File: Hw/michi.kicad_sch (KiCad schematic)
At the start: 52 parts, among them J1 Conn_01x02, J2 Conn_Right, P1 USB_C_Plug_USB2.0, SW1 SW_Push, U1 RP2040, U2 NCP1117ST33T3G, U3 W25Q128JVS, Y1 Crystal

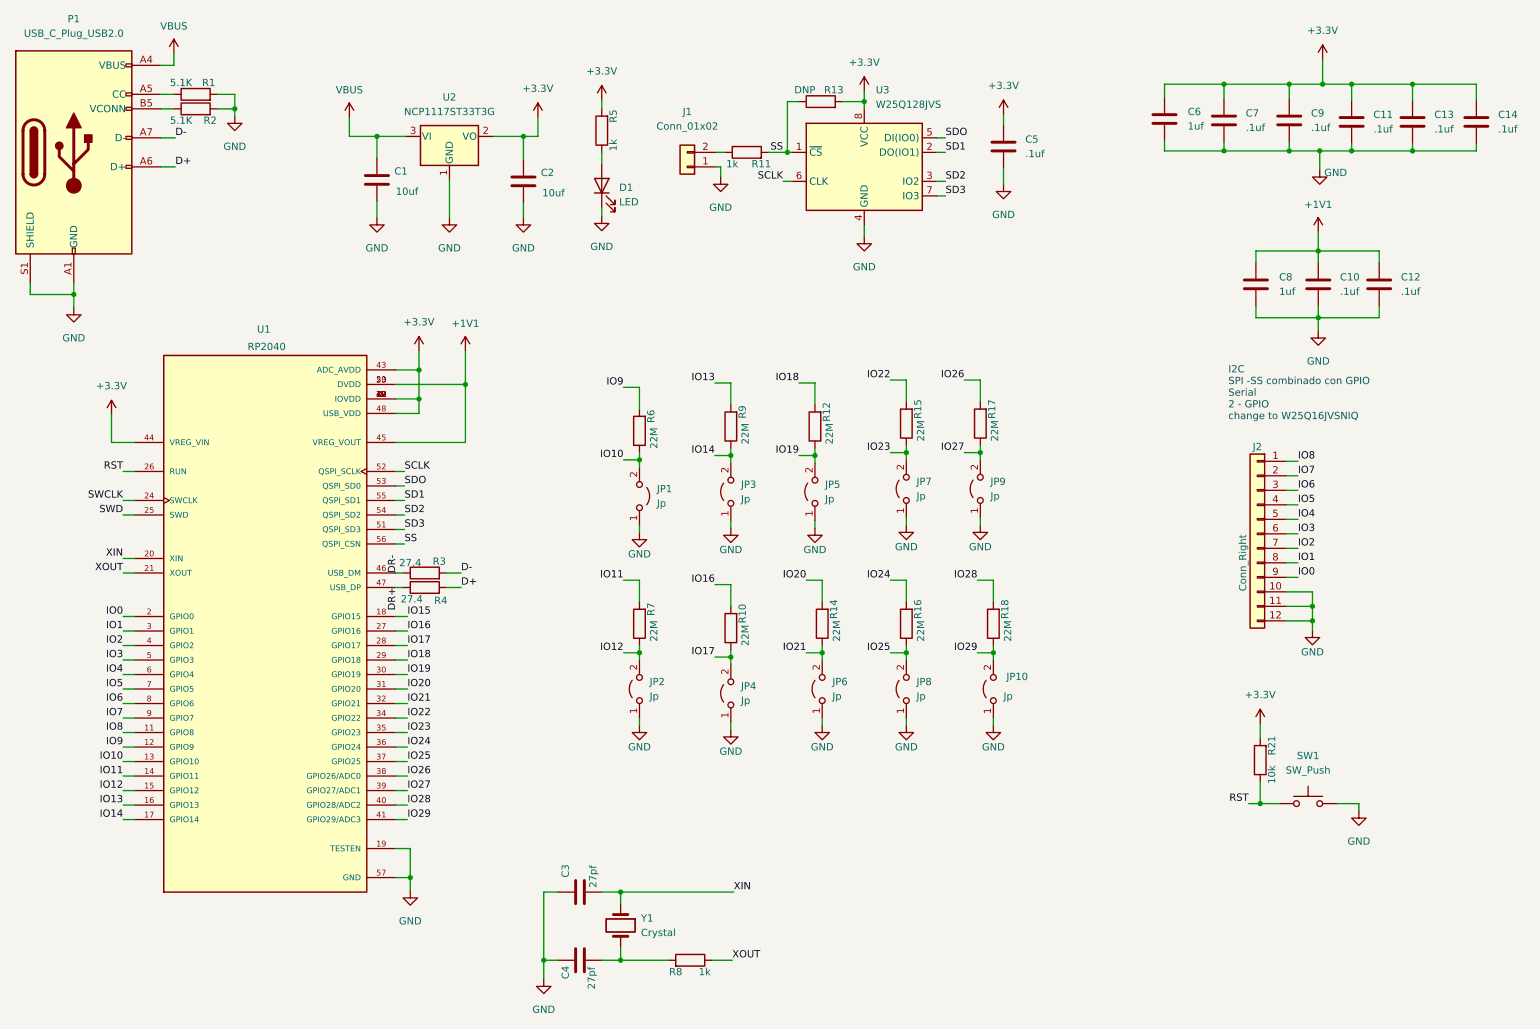
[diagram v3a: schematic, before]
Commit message: fix footprints
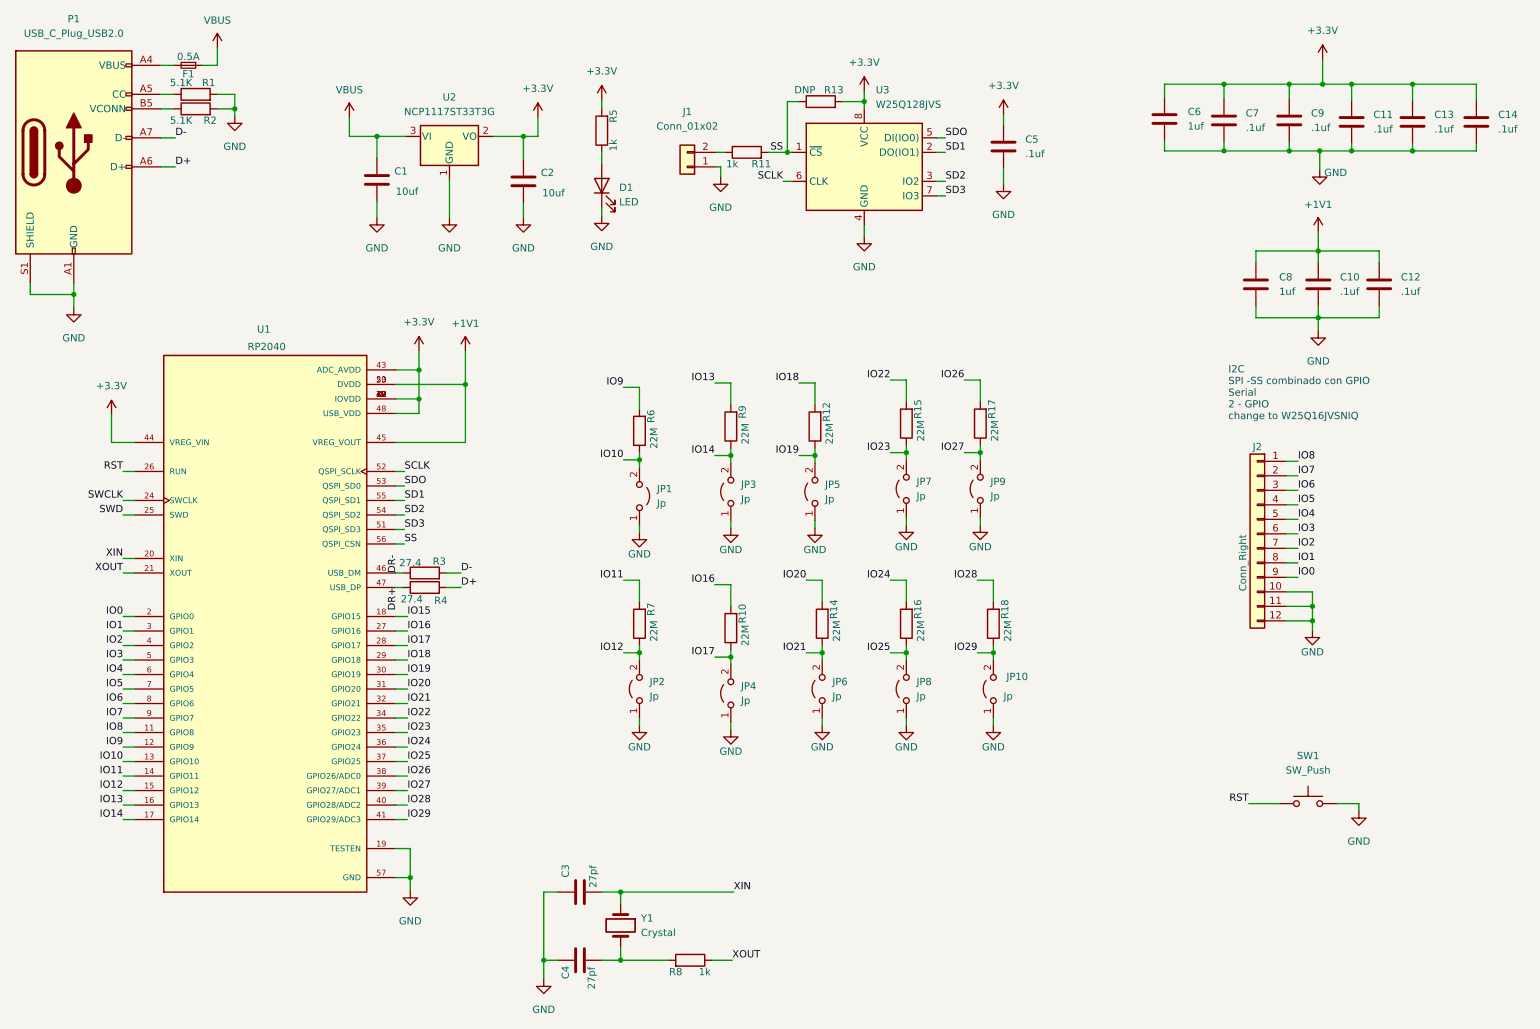
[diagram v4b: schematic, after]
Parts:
- removed R21: 10k, Resistor_SMD:R_0603_1608Metric, symbol Device:R
- added F1: 0.5A, Fuse:Fuse_1812_4532Metric_Pad1.30x3.40mm_HandSolder, symbol Device:Fuse_Small
- U3: footprint Package_SO:SOIC-8_5.23x5.23mm_P1.27mm -> Library:W25Q16JVUUIQ; Manuf W25Q128JVSIM TR -> W25Q16JVUUIQ
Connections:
- net VBUS: now also F1.1; no longer P1.A4 (VBUS), P1.A9 (VBUS), P1.B4 (VBUS), P1.B9 (VBUS)
- new net: F1.2, P1.A4 (VBUS), P1.A9 (VBUS), P1.B4 (VBUS), P1.B9 (VBUS)
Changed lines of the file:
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@@
   (junction (at 245.618 118.364) (diameter 0) (color 0 0 0 0)
   )
-  (junction (at 236.474 152.908) (diameter 0) (color 0 0 0 0)
-  )
   (junction (at 245.618 120.904) (diameter 0) (color 0 0 0 0)
   )
@@
     (stroke (width 0) (type default) (color 0 0 0 0))
   )
+  (wire (pts (xy 53.848 20.574) (xy 53.848 23.622))
+    (stroke (width 0) (type default) (color 0 0 0 0))
+  )
   (wire (pts (xy 241.046 95.504) (xy 243.078 95.504))
     (stroke (width 0) (type default) (color 0 0 0 0))
@@
     (stroke (width 0) (type default) (color 0 0 0 0))
   )
-  (wire (pts (xy 236.474 149.098) (xy 236.474 152.908))
-    (stroke (width 0) (type default) (color 0 0 0 0))
-  )
   (wire (pts (xy 191.516 32.258) (xy 191.516 34.036))
     (stroke (width 0) (type default) (color 0 0 0 0))
@@
     (stroke (width 0) (type default) (color 0 0 0 0))
   )
-  (wire (pts (xy 46.228 23.622) (xy 46.228 21.59))
-    (stroke (width 0) (type default) (color 0 0 0 0))
-  )
   (wire (pts (xy 171.704 78.74) (xy 174.498 78.74))
     (stroke (width 0) (type default) (color 0 0 0 0))
@@
     (stroke (width 0) (type default) (color 0 0 0 0))
   )
+  (wire (pts (xy 53.848 23.622) (xy 51.308 23.622))
+    (stroke (width 0) (type default) (color 0 0 0 0))
+  )
   (wire (pts (xy 127.762 126.492) (xy 127.762 127.762))
     (stroke (width 0) (type default) (color 0 0 0 0))
@@
     (stroke (width 0) (type default) (color 0 0 0 0))
   )
-  (wire (pts (xy 234.442 152.908) (xy 236.474 152.908))
+  (wire (pts (xy 234.442 152.908) (xy 239.776 152.908))
     (stroke (width 0) (type default) (color 0 0 0 0))
   )
@@
     (stroke (width 0) (type default) (color 0 0 0 0))
   )
-  (wire (pts (xy 236.474 152.908) (xy 239.776 152.908))
-    (stroke (width 0) (type default) (color 0 0 0 0))
-  )
   (wire (pts (xy 37.338 132.842) (xy 39.37 132.842))
     (stroke (width 0) (type default) (color 0 0 0 0))
@@
     (stroke (width 0) (type default) (color 0 0 0 0))
   )
-  (wire (pts (xy 236.474 138.938) (xy 236.474 141.478))
-    (stroke (width 0) (type default) (color 0 0 0 0))
-  )
   (wire (pts (xy 85.09 94.742) (xy 86.614 94.742))
     (stroke (width 0) (type default) (color 0 0 0 0))
@@
     (pin "1")
   )
+  (symbol (lib_id "Device:Fuse_Small") (at 48.768 23.622 0) (mirror y) (unit 1)
+    (in_bom yes) (on_board yes)
+    (property "Reference" "F1" (id 0) (at 48.768 25.146 0))
+    (property "Value" "0.5A" (id 1) (at 48.768 22.098 0))
+    (property "Footprint" "Fuse:Fuse_1812_4532Metric_Pad1.30x3.40mm_HandSolder" (id 2) (at 48.768 23.622 0)
+      (effects (font (size 1.27 1.27)) hide)
+    )
+    (property "Datasheet" "" (id 3) (at 48.768 23.622 0))
+    (property "Part#" "" (id 4) (at 48.768 23.622 0)
+      (effects (font (size 1.524 1.524)) hide)
+    )
+    (property "manf#" "0ZCG0030FF2C" (id 5) (at 48.768 23.622 0)
+      (effects (font (size 1.27 1.27)) hide)
+    )
+    (property "Supplier " "Mouser" (id 6) (at 48.768 23.622 0)
+      (effects (font (size 1.27 1.27)) hide)
+    )
+    (pin "1")
+    (pin "2")
+  )
   (symbol (lib_id "Device:C") (at 191.516 37.846 0) (unit 1)
     (in_bom yes) (on_board yes) (fields_autoplaced)
@@
   (symbol (lib_id "power:GND") (at 245.618 122.555 0) (unit 1)
     (in_bom yes) (on_board yes)
-    (property "Reference" "#PWR?" (id 0) (at 245.618 128.905 0)
+    (property "Reference" "#PWR0103" (id 0) (at 245.618 128.905 0)
       (effects (font (size 1.27 1.27)) hide)
     )
@@
       (effects (font (size 1.27 1.27)) (justify left))
     )
-    (property "Footprint" "Package_SO:SOIC-8_5.23x5.23mm_P1.27mm" (id 2) (at 167.132 41.402 0)
+    (property "Footprint" "Library:W25Q16JVUUIQ" (id 2) (at 167.132 41.402 0)
       (effects (font (size 1.27 1.27)) hide)
     )
@@
       (effects (font (size 1.27 1.27)) hide)
     )
-    (property "Manuf" "W25Q128JVSIM TR" (id 4) (at 167.132 41.402 0)
+    (property "Manuf" "W25Q16JVUUIQ" (id 4) (at 167.132 41.402 0)
       (effects (font (size 1.27 1.27)) hide)
     )
@@
     (pin "2")
   )
-  (symbol (lib_id "power:VBUS") (at 46.228 21.59 0) (unit 1)
+  (symbol (lib_id "power:VBUS") (at 53.848 20.574 0) (unit 1)
     (in_bom yes) (on_board yes) (fields_autoplaced)
-    (property "Reference" "#PWR03" (id 0) (at 46.228 25.4 0)
+    (property "Reference" "#PWR03" (id 0) (at 53.848 24.384 0)
       (effects (font (size 1.27 1.27)) hide)
     )
-    (property "Value" "VBUS" (id 1) (at 46.228 16.764 0))
-    (property "Footprint" "" (id 2) (at 46.228 21.59 0)
+    (property "Value" "VBUS" (id 1) (at 53.848 15.748 0))
+    (property "Footprint" "" (id 2) (at 53.848 20.574 0)
       (effects (font (size 1.27 1.27)) hide)
     )
-    (property "Datasheet" "" (id 3) (at 46.228 21.59 0)
+    (property "Datasheet" "" (id 3) (at 53.848 20.574 0)
       (effects (font (size 1.27 1.27)) hide)
     )
@@
     (pin "2")
   )
-  (symbol (lib_id "power:+3.3V") (at 236.474 138.938 0) (unit 1)
-    (in_bom yes) (on_board yes) (fields_autoplaced)
-    (property "Reference" "#PWR0102" (id 0) (at 236.474 142.748 0)
-      (effects (font (size 1.27 1.27)) hide)
-    )
-    (property "Value" "+3.3V" (id 1) (at 236.474 133.858 0))
-    (property "Footprint" "" (id 2) (at 236.474 138.938 0)
-      (effects (font (size 1.27 1.27)) hide)
-    )
-    (property "Datasheet" "" (id 3) (at 236.474 138.938 0)
-      (effects (font (size 1.27 1.27)) hide)
-    )
-    (pin "1")
-  )
   (symbol (lib_id "power:GND") (at 167.132 53.594 0) (unit 1)
     (in_bom yes) (on_board yes) (fields_autoplaced)
@@
     (pin "1")
   )
-  (symbol (lib_id "Device:R") (at 236.474 145.288 180) (unit 1)
-    (in_bom yes) (on_board yes)
-    (property "Reference" "R21" (id 0) (at 238.506 142.748 90))
-    (property "Value" "10k" (id 1) (at 238.506 147.828 90))
-    (property "Footprint" "Resistor_SMD:R_0603_1608Metric" (id 2) (at 238.252 145.288 90)
-      (effects (font (size 1.27 1.27)) hide)
-    )
-    (property "Datasheet" "~" (id 3) (at 236.474 145.288 0)
-      (effects (font (size 1.27 1.27)) hide)
-    )
-    (property "#LCSC" "C217281" (id 4) (at 236.474 145.288 0)
-      (effects (font (size 1.27 1.27)) hide)
-    )
-    (property "Manuf" "CR-03JL7---10K" (id 5) (at 236.474 145.288 0)
-      (effects (font (size 1.27 1.27)) hide)
-    )
-    (property "MANUFACTURER" "LCSC" (id 6) (at 236.474 145.288 0)
-      (effects (font (size 1.27 1.27)) hide)
-    )
-    (pin "1")
-    (pin "2")
-  )
   (symbol (lib_id "power:+3.3V") (at 89.154 73.66 0) (unit 1)
     (in_bom yes) (on_board yes) (fields_autoplaced)
@@
       (reference "#PWR0101") (unit 1) (value "GND") (footprint "")
     )
-    (path "/b3206de0-c8bc-4a86-8b87-d7481ab74d64"
-      (reference "#PWR0102") (unit 1) (value "+3.3V") (footprint "")
-    )
     (path "/51922175-4c44-4a31-bb11-efc74e3866fe"
-      (reference "#PWR?") (unit 1) (value "GND") (footprint "")
+      (reference "#PWR0103") (unit 1) (value "GND") (footprint "")
     )
     (path "/6c00fb26-6a97-4b66-9ca0-7145f81dd24b"
@@
       (reference "D1") (unit 1) (value "LED") (footprint "Diode_SMD:D_0805_2012Metric")
     )
+    (path "/2f13a951-3323-4ff5-a8f0-c41f06433742"
+      (reference "F1") (unit 1) (value "0.5A") (footprint "Fuse:Fuse_1812_4532Metric_Pad1.30x3.40mm_HandSolder")
+    )
     (path "/ccde2508-fbdf-423f-99e7-7ae8b33bc4e0"
       (reference "J1") (unit 1) (value "Conn_01x02") (footprint "Connector_PinSocket_2.54mm:PinSocket_1x02_P2.54mm_Vertical")
@@
       (reference "R18") (unit 1) (value "22M ") (footprint "Resistor_SMD:R_0603_1608Metric")
     )
-    (path "/fb9d77c1-b24e-4f4c-be18-7037fa4b11f1"
-      (reference "R21") (unit 1) (value "10k") (footprint "Resistor_SMD:R_0603_1608Metric")
-    )
     (path "/49ae2230-f2ce-4cfe-92b1-5f039fbe40b1"
       (reference "SW1") (unit 1) (value "SW_Push") (footprint "Button_Switch_SMD:SW_SPST_TL3342")
@@
     )
     (path "/61514653-1401-4f5a-aafd-66d24c8d8ff6"
-      (reference "U3") (unit 1) (value "W25Q128JVS") (footprint "Package_SO:SOIC-8_5.23x5.23mm_P1.27mm")
+      (reference "U3") (unit 1) (value "W25Q128JVS") (footprint "Library:W25Q16JVUUIQ")
     )
     (path "/607bdbd7-2bc0-4755-9567-52567bf1a6e1"

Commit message: update v1.0 layout
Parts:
- JP10: value Jp -> LEFT
- JP3: value Jp -> A
- JP4: value Jp -> W
- JP5: value Jp -> SPACE
- JP6: value Jp -> Click
- JP7: value Jp -> RIGHT
- JP8: value Jp -> DOWN
- JP9: value Jp -> UP
- R13: footprint Resistor_SMD:R_0603_1608Metric -> (none)
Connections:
- net +3V3: now also J2.10 (Pin_10)
- net GND: no longer D1.1 (K), J2.10 (Pin_10)
- net IO15: now also D1.1 (K)
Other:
- moved on the sheet: JP10, JP5, JP6, JP7, JP8, JP9, R12, R14, R15, R16, R17, R18

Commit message: Update BOM
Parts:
- F1: #LCSC (none) -> 0ZCG0030FF2C; MANUFACTURER (none) -> Mouser
- J2: #LCSC (none) -> 61001211921
- P1: #LCSC (none) -> C393939
- U1: #LCSC (none) -> RP2040
- U2: #LCSC (none) -> NCP1117ST33T3G
- U3: #LCSC (none) -> W25Q128JVSIM TR
- Y1: #LCSC (none) -> ECS-120-18-30-JGN-TR
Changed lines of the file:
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@@
+      (effects (font (size 1.27 1.27)) hide)
+    )
+    (property "#LCSC" "0ZCG0030FF2C" (id 7) (at 48.768 23.622 0)
+      (effects (font (size 1.27 1.27)) hide)
+    )
+    (property "MANUFACTURER" "Mouser" (id 8) (at 48.768 23.622 0)
       (effects (font (size 1.27 1.27)) hide)
     )
@@
       (effects (font (size 1.27 1.27)) hide)
     )
+    (property "#LCSC" "ECS-120-18-30-JGN-TR" (id 6) (at 124.46 174.244 0)
+      (effects (font (size 1.27 1.27)) hide)
+    )
     (pin "1")
     (pin "2")
@@
     )
     (property "MANUFACTURER" "Mouser " (id 5) (at 167.132 41.402 0)
+      (effects (font (size 1.27 1.27)) hide)
+    )
+    (property "#LCSC" "W25Q128JVSIM TR" (id 6) (at 167.132 41.402 0)
       (effects (font (size 1.27 1.27)) hide)
     )
@@
     )
     (property "Manuf" "RP2040" (id 8) (at 62.23 122.682 0)
+      (effects (font (size 1.27 1.27)) hide)
+    )
+    (property "#LCSC" "RP2040" (id 9) (at 62.23 122.682 0)
       (effects (font (size 1.27 1.27)) hide)
     )
@@
       (effects (font (size 1.27 1.27)) hide)
     )
+    (property "#LCSC" "61001211921" (id 5) (at 235.966 105.664 0)
+      (effects (font (size 1.27 1.27)) hide)
+    )
     (pin "1")
     (pin "10")
@@
     )
     (property "MANUFACTURER" "Mouser " (id 5) (at 28.702 38.862 0)
+      (effects (font (size 1.27 1.27)) hide)
+    )
+    (property "#LCSC" "C393939" (id 6) (at 28.702 38.862 0)
       (effects (font (size 1.27 1.27)) hide)
     )
@@
       (effects (font (size 1.27 1.27)) hide)
     )
+    (property "#LCSC" "NCP1117ST33T3G" (id 6) (at 94.488 36.068 0)
+      (effects (font (size 1.27 1.27)) hide)
+    )

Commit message: Update labels schematic
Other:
- note added: "A"
- note added: "D"
- note added: "DOWN"
- note added: "LEFT"
- note added: "MOUSE"
- note added: "RIGHT"
- note added: "S"
- note added: "SPACE"
- note added: "UP"
- note added: "W"
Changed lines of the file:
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@@
     (stroke (width 0) (type default) (color 0 0 0 0))
+  )
+  (text "MOUSE" (at 175.895 129.286 0)
+    (effects (font (size 2 2) bold) (justify left bottom))
+  )
+  (text "LEFT" (at 218.186 125.349 0)
+    (effects (font (size 2 2) bold) (justify left bottom))
+  )
+  (text "SPACE" (at 174.498 94.615 0)
+    (effects (font (size 2 2) bold) (justify left bottom))
+  )
+  (text "S" (at 117.348 126.492 0)
+    (effects (font (size 2 2) bold) (justify left bottom))
+  )
+  (text "A" (at 148.971 93.218 0)
+    (effects (font (size 2 2) bold) (justify left bottom))
+  )
+  (text "D" (at 116.205 93.726 0)
+    (effects (font (size 2 2) (thickness 0.4) bold) (justify left bottom))
   )
   (text "I2C\nSPI -SS combinado con GPIO\nSerial\n2 - GPIO\nchange to W25Q16JVSNIQ"
@@
     (effects (font (size 1.27 1.27)) (justify left bottom))
   )
+  (text "RIGHT" (at 190.627 77.978 0)
+    (effects (font (size 2 2) bold) (justify left bottom))
+  )
+  (text "UP" (at 215.011 95.25 0)
+    (effects (font (size 2 2) bold) (justify left bottom))
+  )
+  (text "DOWN" (at 198.882 141.859 0)
+    (effects (font (size 2 2) bold) (justify left bottom))
+  )
+  (text "W" (at 149.86 127.381 0)
+    (effects (font (size 2 2) bold) (justify left bottom))
+  )
   (label "IO11" (at 37.338 148.082 180)

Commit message: change R3 & R4 #manf for stock
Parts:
- R3: value 27.4 -> 27; #LCSC C177713 -> C25190; Manuf RCT0327R4FLF -> 0603WAF270JT5E
- R4: #LCSC C177713 -> C25190; Manuf RCT0327R4FLF -> 0603WAF270JT5E
